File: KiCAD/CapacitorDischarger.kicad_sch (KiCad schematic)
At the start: 43 parts, among them J1 SLB4-G-21, J2 SLB4-G-22, J3 MKDS5/2-9.5, J4 MKDS5/2-9.5, J5 DVM_Connector, Q1 2N3904, Q2 STF7NM80 800V 6A

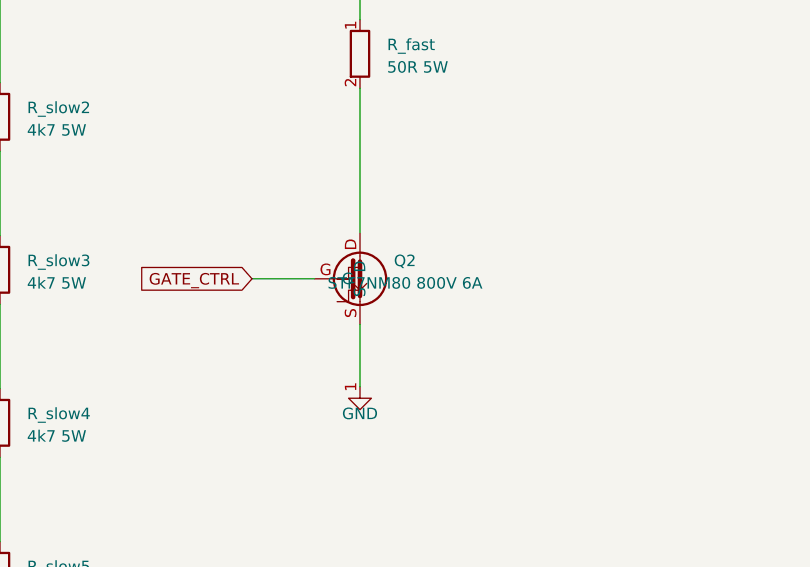
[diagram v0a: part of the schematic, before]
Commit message: Update Q2 to STP10NK80Z across schematics, SVG, and CSV
- KiCAD/hv_section.kicad_sch: Q2 value STF7NM80 → STP10NK80Z
- KiCAD/CapacitorDischarger.kicad_sch: Q2 value updated to STP10NK80Z 800V 9A
- blocks/gen_full_schematic.py: branch 2 comment updated
- blocks/full_schematic.svg: regenerated with STP10NK80Z label
- TO_BUY_list.csv: Q2 primary updated to STP10NK80Z

Simulation files retain STF7NM80 SPICE model — functionally equivalent.

Co-Authored-By: Claude Sonnet 4.6 <noreply@anthropic.com>
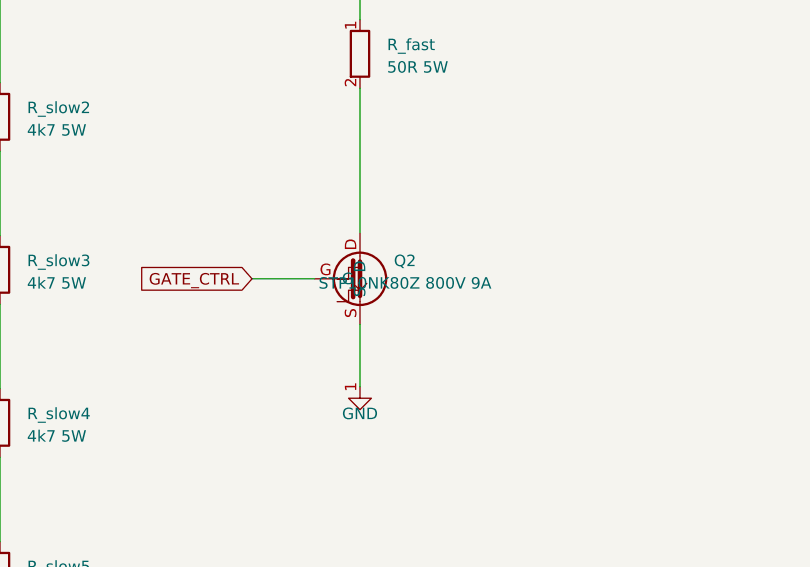
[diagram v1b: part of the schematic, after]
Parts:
- Q2: value STF7NM80 800V 6A -> STP10NK80Z 800V 9A
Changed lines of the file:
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@@
   (symbol (lib_id "Device:Q_NMOS_GDS") (at 160 80 0) (unit 1) (in_bom yes) (on_board yes)
     (property "Reference" "Q2" (at 165 78 0) (effects (font (size 1.27 1.27))))
-    (property "Value" "STF7NM80 800V 6A" (at 165 80.5 0) (effects (font (size 1.27 1.27))))
+    (property "Value" "STP10NK80Z 800V 9A" (at 165 80.5 0) (effects (font (size 1.27 1.27))))
     (property "Footprint" "Package_TO_SOT_THT:TO-220-3_Vertical" (at 0 0 0) (effects (font (size 1.27 1.27)) hide))
     (property "Datasheet" "" (at 0 0 0) (effects (font (size 1.27 1.27)) hide))

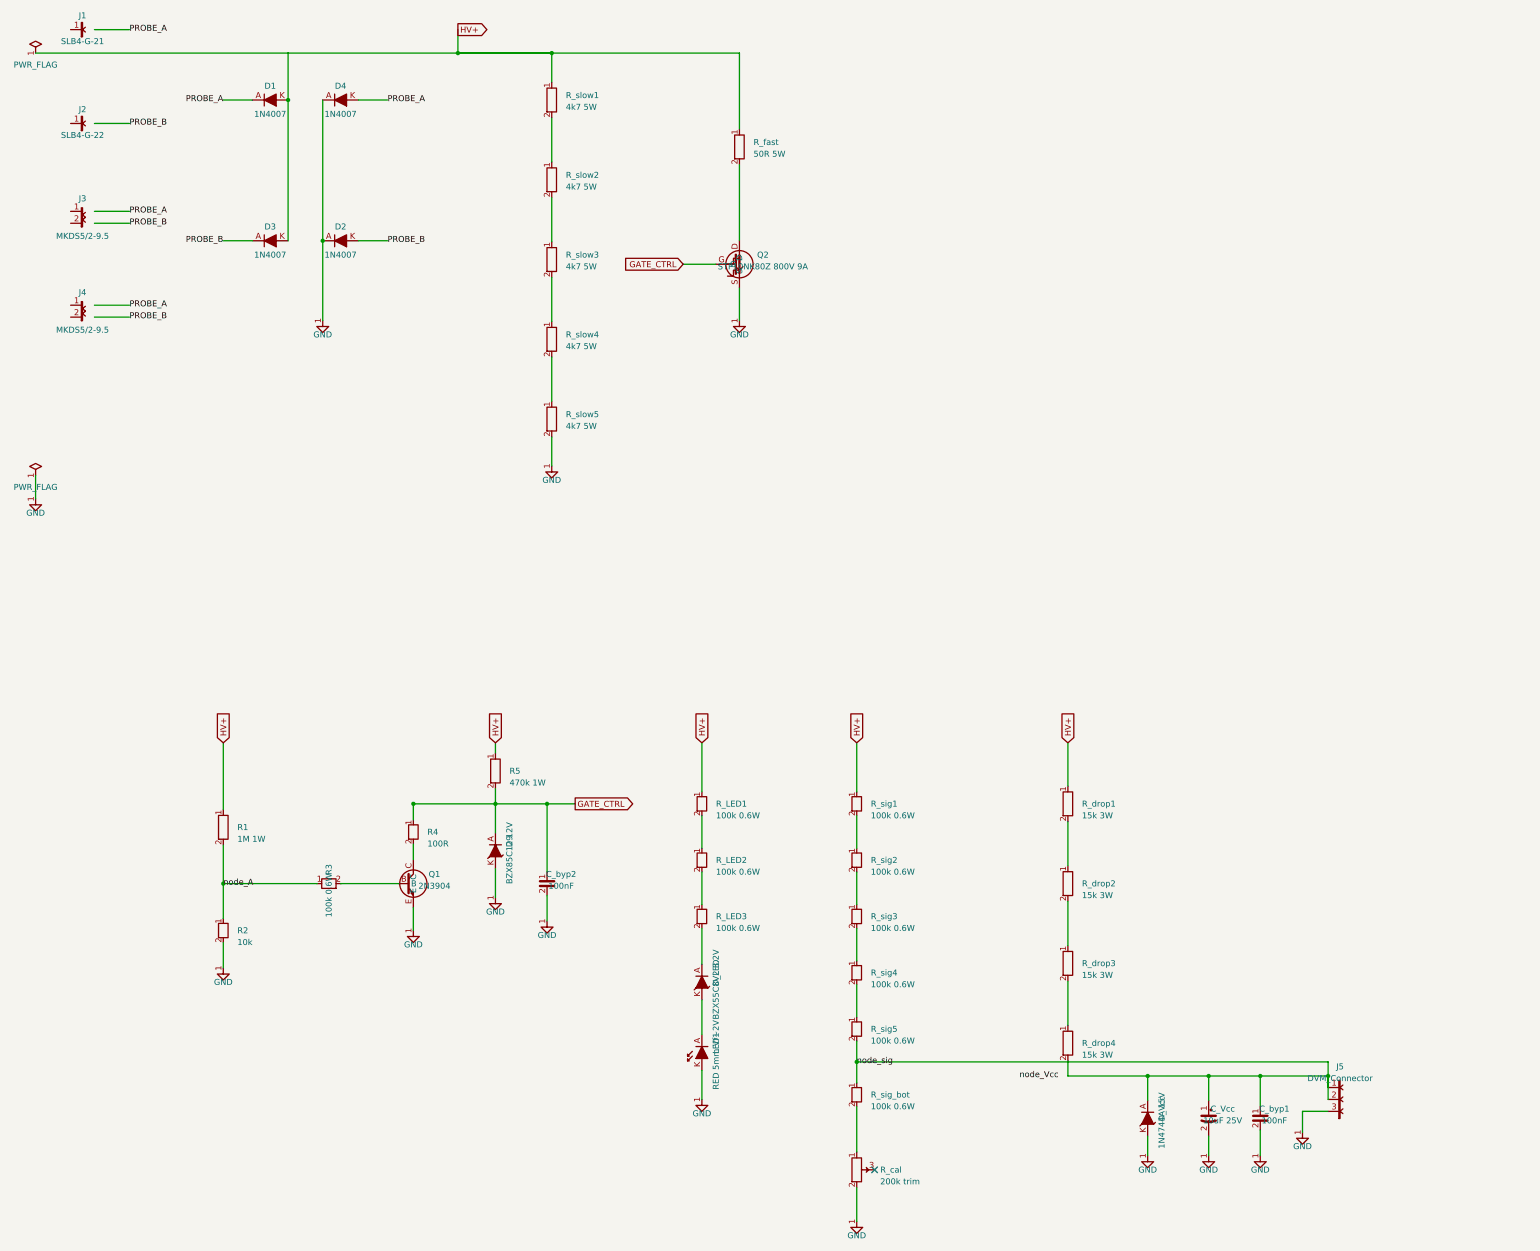
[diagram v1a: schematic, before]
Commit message: Update main KiCAD schematic: MPSA42, R_LED4, 10k trimmer
- Q1 value: 2N3904 → MPSA42
- R_cal value: 200k trim → 10k trim
- LED chain: add R_LED4 symbol + connecting wire; shift D_LED,
  LED1 and GND down 12 units to accommodate the extra resistor

Co-Authored-By: Claude Sonnet 4.6 <noreply@anthropic.com>
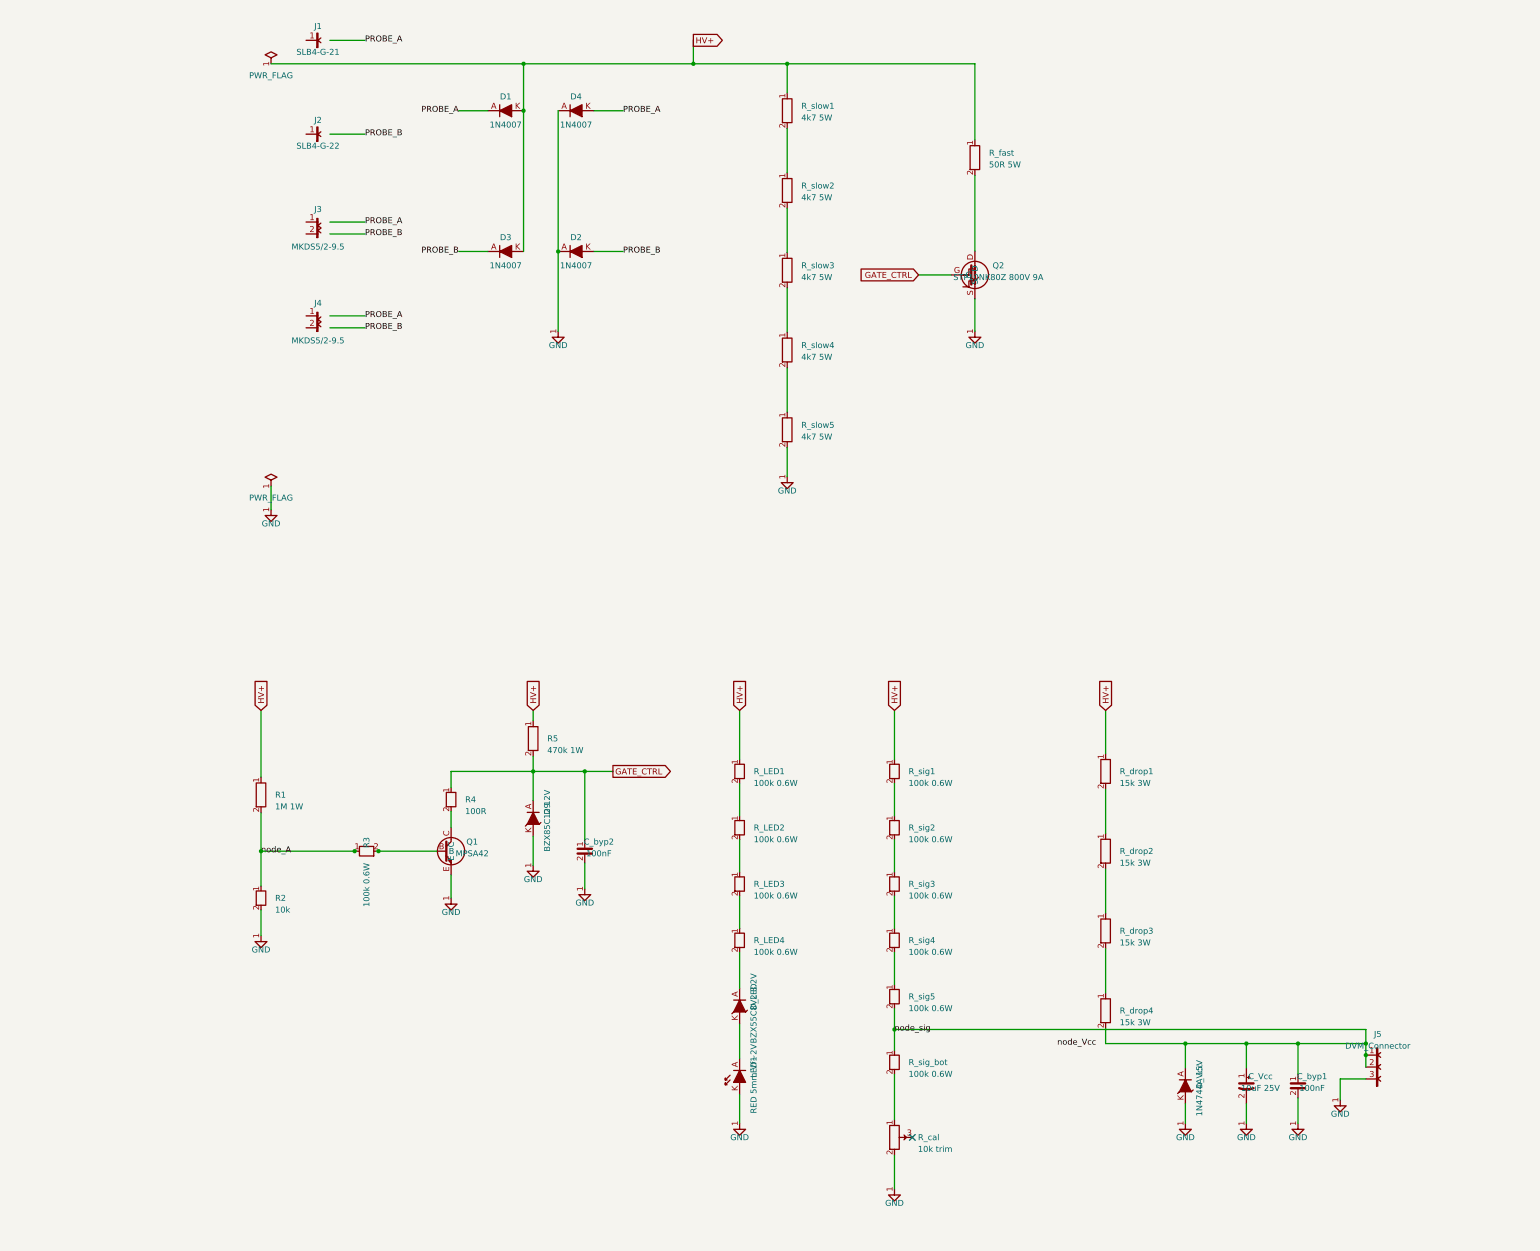
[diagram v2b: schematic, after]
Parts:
- added R_LED4: 100k 0.6W, Resistor_THT:R_Axial_DIN0207_L6.3mm_D2.5mm_P10.16mm_Horizontal, symbol Device:R
- Q1: value 2N3904 -> MPSA42
- R_cal: value 200k trim -> 10k trim
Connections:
- net node_A: now also R3.1
- net at R3.2: now also Q1.B
- net at R_LED3.2: now also R_LED4.1; no longer D_LED.A
- new net: D_LED.A, R_LED4.2
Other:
- moved on the sheet: C_Vcc, C_byp1, C_byp2, D1, D2, D3, D4, D9, D_LED, D_Vcc, J1, J2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

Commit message: Fix footprints to match KiCad 10 library and actual sourced components
Five footprint names didn't exist in KiCad 10 (caused 'Cannot add' errors),
and R_slow/R_fast were sized for generic ceramics, not the actual Ohmite parts.

Library name fixes (all three schematics):
  R_Axial_Power_L15mm_W5mm_P20.32mm   → R_Axial_DIN0516_L15.5mm_D5.0mm_P20.32mm_Horizontal
  C_Disc_D3.8mm_W2.6mm_P5.00mm        → C_Disc_D3.8mm_W2.6mm_P2.50mm
  CP_Radial_D4.0mm_P2.50mm            → CP_Radial_D4.0mm_P2.00mm
  Potentiometer_Vishay_T93_Vertical    → Potentiometer_Bourns_3296W_Vertical

Correct sizing for sourced Ohmite wirewound resistors:
  R_slow1-5 (Ohmite 45F, 5W, body 23.8×8.7mm) → R_Axial_Power_L25.0mm_W9.0mm_P30.48mm
  R_fast     (Ohmite 27J, 7W, body 32.1×10mm)  → R_Axial_Power_L38.0mm_W9.0mm_P40.64mm

Co-Authored-By: Claude Sonnet 4.6 <noreply@anthropic.com>
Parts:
- C_Vcc: footprint Capacitor_THT:CP_Radial_D4.0mm_P2.50mm -> Capacitor_THT:CP_Radial_D4.0mm_P2.00mm
- C_byp1, C_byp2: footprint Capacitor_THT:C_Disc_D3.8mm_W2.6mm_P5.00mm -> Capacitor_THT:C_Disc_D3.8mm_W2.6mm_P2.50mm
- R1, R5, R_drop1, R_drop2, R_drop3, R_drop4: footprint Resistor_THT:R_Axial_Power_L15mm_W5mm_P20.32mm -> Resistor_THT:R_Axial_DIN0516_L15.5mm_D5.0mm_P20.32mm_Horizontal
- R_cal: footprint Potentiometer_THT:Potentiometer_Vishay_T93_Vertical -> Potentiometer_THT:Potentiometer_Bourns_3296W_Vertical
- R_fast: footprint Resistor_THT:R_Axial_Power_L38mm_W10mm_P41.91mm -> Resistor_THT:R_Axial_Power_L38.0mm_W9.0mm_P40.64mm
- R_slow1, R_slow2, R_slow3, R_slow4, R_slow5: footprint Resistor_THT:R_Axial_Power_L38mm_W10mm_P41.91mm -> Resistor_THT:R_Axial_Power_L25.0mm_W9.0mm_P30.48mm
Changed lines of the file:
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@@
 			)
 		)
-		(property "Footprint" "Resistor_THT:R_Axial_Power_L38mm_W10mm_P41.91mm"
+		(property "Footprint" "Resistor_THT:R_Axial_Power_L25.0mm_W9.0mm_P30.48mm"
 			(at 50.18 2.28 0)
 			(hide yes)
@@
 			)
 		)
-		(property "Footprint" "Resistor_THT:R_Axial_Power_L38mm_W10mm_P41.91mm"
+		(property "Footprint" "Resistor_THT:R_Axial_Power_L25.0mm_W9.0mm_P30.48mm"
 			(at 50.18 2.28 0)
 			(hide yes)
@@
 			)
 		)
-		(property "Footprint" "Resistor_THT:R_Axial_Power_L38mm_W10mm_P41.91mm"
+		(property "Footprint" "Resistor_THT:R_Axial_Power_L25.0mm_W9.0mm_P30.48mm"
 			(at 50.18 2.28 0)
 			(hide yes)
@@
 			)
 		)
-		(property "Footprint" "Resistor_THT:R_Axial_Power_L38mm_W10mm_P41.91mm"
+		(property "Footprint" "Resistor_THT:R_Axial_Power_L25.0mm_W9.0mm_P30.48mm"
 			(at 50.18 2.28 0)
 			(hide yes)
@@
 			)
 		)
-		(property "Footprint" "Resistor_THT:R_Axial_Power_L38mm_W10mm_P41.91mm"
+		(property "Footprint" "Resistor_THT:R_Axial_Power_L25.0mm_W9.0mm_P30.48mm"
 			(at 50.18 2.28 0)
 			(hide yes)
@@
 			)
 		)
-		(property "Footprint" "Resistor_THT:R_Axial_Power_L38mm_W10mm_P41.91mm"
+		(property "Footprint" "Resistor_THT:R_Axial_Power_L38.0mm_W9.0mm_P40.64mm"
 			(at 50.18 2.28 0)
 			(hide yes)
@@
 			)
 		)
-		(property "Footprint" "Resistor_THT:R_Axial_Power_L15mm_W5mm_P20.32mm"
+		(property "Footprint" "Resistor_THT:R_Axial_DIN0516_L15.5mm_D5.0mm_P20.32mm_Horizontal"
 			(at 8.04 -6.91 0)
 			(hide yes)
@@
 			)
 		)
-		(property "Footprint" "Resistor_THT:R_Axial_Power_L15mm_W5mm_P20.32mm"
+		(property "Footprint" "Resistor_THT:R_Axial_DIN0516_L15.5mm_D5.0mm_P20.32mm_Horizontal"
 			(at 8.04 -6.91 0)
 			(hide yes)
@@
 			)
 		)
-		(property "Footprint" "Capacitor_THT:C_Disc_D3.8mm_W2.6mm_P5.00mm"
+		(property "Footprint" "Capacitor_THT:C_Disc_D3.8mm_W2.6mm_P2.50mm"
 			(at 8.04 -6.91 0)
 			(hide yes)
@@
 			)
 		)
-		(property "Footprint" "Potentiometer_THT:Potentiometer_Vishay_T93_Vertical"
+		(property "Footprint" "Potentiometer_THT:Potentiometer_Bourns_3296W_Vertical"
 			(at 8.04 -6.91 0)
 			(hide yes)
@@
 			)
 		)
-		(property "Footprint" "Resistor_THT:R_Axial_Power_L15mm_W5mm_P20.32mm"
+		(property "Footprint" "Resistor_THT:R_Axial_DIN0516_L15.5mm_D5.0mm_P20.32mm_Horizontal"
 			(at 8.04 -6.91 0)
 			(hide yes)
@@
 			)
 		)
-		(property "Footprint" "Resistor_THT:R_Axial_Power_L15mm_W5mm_P20.32mm"
+		(property "Footprint" "Resistor_THT:R_Axial_DIN0516_L15.5mm_D5.0mm_P20.32mm_Horizontal"
 			(at 8.04 -6.91 0)
 			(hide yes)
@@
 			)
 		)
-		(property "Footprint" "Resistor_THT:R_Axial_Power_L15mm_W5mm_P20.32mm"
+		(property "Footprint" "Resistor_THT:R_Axial_DIN0516_L15.5mm_D5.0mm_P20.32mm_Horizontal"
 			(at 8.04 -6.91 0)
 			(hide yes)
@@
 			)
 		)
-		(property "Footprint" "Resistor_THT:R_Axial_Power_L15mm_W5mm_P20.32mm"
+		(property "Footprint" "Resistor_THT:R_Axial_DIN0516_L15.5mm_D5.0mm_P20.32mm_Horizontal"
 			(at 8.04 -6.91 0)
 			(hide yes)
@@
 			)
 		)
-		(property "Footprint" "Capacitor_THT:CP_Radial_D4.0mm_P2.50mm"
+		(property "Footprint" "Capacitor_THT:CP_Radial_D4.0mm_P2.00mm"
 			(at 8.04 -6.91 0)
 			(hide yes)
@@
 			)
 		)
-		(property "Footprint" "Capacitor_THT:C_Disc_D3.8mm_W2.6mm_P5.00mm"
+		(property "Footprint" "Capacitor_THT:C_Disc_D3.8mm_W2.6mm_P2.50mm"
 			(at 8.04 -6.91 0)
 			(hide yes)
